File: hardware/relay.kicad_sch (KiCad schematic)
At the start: 0 parts

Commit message: Relay module completed
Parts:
- added D?: 1N4148, Diode_THT:D_DO-35_SOD27_P7.62mm_Horizontal, symbol Diode:1N4148
- added D?: LED_GREEN, symbol Device:LED
- added K?: G5LE-1, Relay_THT:Relay_SPDT_Omron-G5LE-1, symbol Relay:G5LE-1
- added Q?: BC847, Package_TO_SOT_SMD:SOT-23, symbol Transistor_BJT:BC847
- added R? (x2): 4K7, symbol Device:R_Small
- added R?: 47K, symbol Device:R_Small
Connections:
- new net: Q?.1 (B), R?.1, R?.2
- new net: D?.2 (A), K?.2, Q?.3 (C), R?.2
- new net: D?.2 (A), R?.1
- new net +12V: D?.1 (K), K?.5
- new net GND: D?.1 (K), Q?.2 (E), R?.2
- new net RELAY_CNT: R?.1
- new net RELAY_IN: K?.1
- new net RELAY_NC: K?.4
- new net RELAY_NO: K?.3

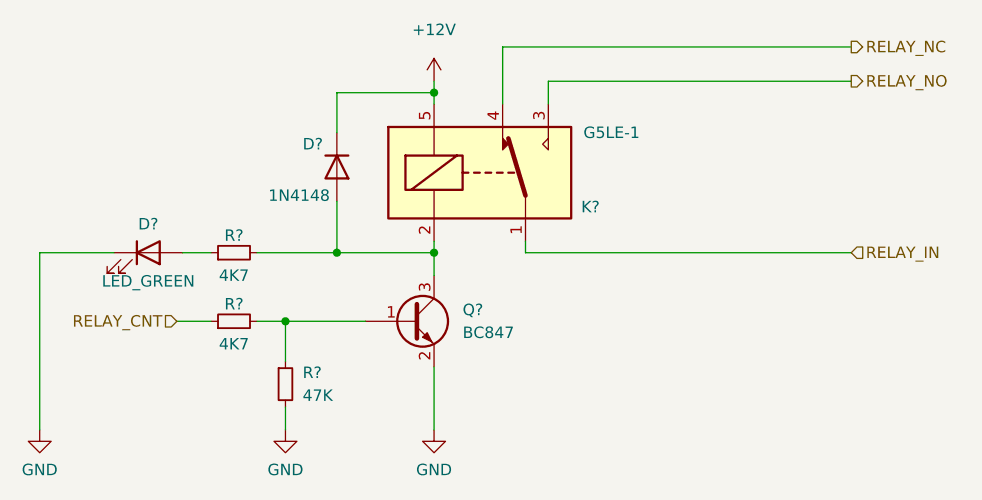
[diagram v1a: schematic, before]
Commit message: Display circuit added
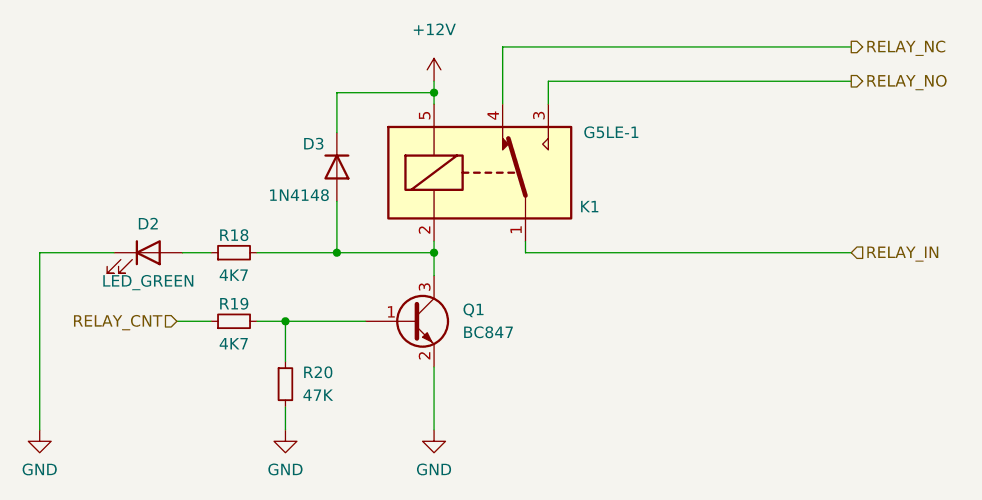
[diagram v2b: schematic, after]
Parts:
- gave numbers to parts that had none: 7
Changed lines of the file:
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@@
   (symbol (lib_id "power:GND") (at 109.22 107.95 0) (unit 1)
     (in_bom yes) (on_board yes) (fields_autoplaced)
-    (property "Reference" "#PWR?" (id 0) (at 109.22 114.3 0)
+    (property "Reference" "#PWR021" (id 0) (at 109.22 114.3 0)
       (effects (font (size 1.27 1.27)) hide)
     )
@@
   (symbol (lib_id "power:+12V") (at 153.035 69.215 0) (unit 1)
     (in_bom yes) (on_board yes) (fields_autoplaced)
-    (property "Reference" "#PWR?" (id 0) (at 153.035 73.025 0)
+    (property "Reference" "#PWR023" (id 0) (at 153.035 73.025 0)
       (effects (font (size 1.27 1.27)) hide)
     )
@@
   (symbol (lib_id "Device:R_Small") (at 130.81 95.885 90) (unit 1)
     (in_bom yes) (on_board yes)
-    (property "Reference" "R?" (id 0) (at 130.81 93.98 90))
+    (property "Reference" "R19" (id 0) (at 130.81 93.98 90))
     (property "Value" "4K7" (id 1) (at 130.81 98.425 90))
     (property "Footprint" "" (id 2) (at 130.81 95.885 0)
@@
   (symbol (lib_id "Relay:G5LE-1") (at 158.115 79.375 0) (unit 1)
     (in_bom yes) (on_board yes)
-    (property "Reference" "K?" (id 0) (at 171.45 83.185 0)
+    (property "Reference" "K1" (id 0) (at 171.45 83.185 0)
       (effects (font (size 1.27 1.27)) (justify right))
     )
@@
   (symbol (lib_id "Diode:1N4148") (at 142.24 78.74 270) (unit 1)
     (in_bom yes) (on_board yes)
-    (property "Reference" "D?" (id 0) (at 138.43 76.2 90)
+    (property "Reference" "D3" (id 0) (at 138.43 76.2 90)
       (effects (font (size 1.27 1.27)) (justify left))
     )
@@
   (symbol (lib_id "power:GND") (at 153.035 107.95 0) (unit 1)
     (in_bom yes) (on_board yes) (fields_autoplaced)
-    (property "Reference" "#PWR?" (id 0) (at 153.035 114.3 0)
+    (property "Reference" "#PWR024" (id 0) (at 153.035 114.3 0)
       (effects (font (size 1.27 1.27)) hide)
     )
@@
   (symbol (lib_id "Transistor_BJT:BC847") (at 150.495 95.885 0) (unit 1)
     (in_bom yes) (on_board yes) (fields_autoplaced)
-    (property "Reference" "Q?" (id 0) (at 156.21 94.6149 0)
+    (property "Reference" "Q1" (id 0) (at 156.21 94.6149 0)
       (effects (font (size 1.27 1.27)) (justify left))
     )
@@
   (symbol (lib_id "Device:LED") (at 121.285 88.265 0) (unit 1)
     (in_bom yes) (on_board yes)
-    (property "Reference" "D?" (id 0) (at 121.285 85.09 0))
+    (property "Reference" "D2" (id 0) (at 121.285 85.09 0))
     (property "Value" "LED_GREEN" (id 1) (at 121.285 91.44 0))
     (property "Footprint" "" (id 2) (at 121.285 88.265 0)
@@
   (symbol (lib_id "power:GND") (at 136.525 107.95 0) (unit 1)
     (in_bom yes) (on_board yes) (fields_autoplaced)
-    (property "Reference" "#PWR?" (id 0) (at 136.525 114.3 0)
+    (property "Reference" "#PWR022" (id 0) (at 136.525 114.3 0)
       (effects (font (size 1.27 1.27)) hide)
     )
@@
   (symbol (lib_id "Device:R_Small") (at 136.525 102.87 0) (unit 1)
     (in_bom yes) (on_board yes) (fields_autoplaced)
-    (property "Reference" "R?" (id 0) (at 138.43 101.5999 0)
+    (property "Reference" "R20" (id 0) (at 138.43 101.5999 0)
       (effects (font (size 1.27 1.27)) (justify left))
     )
@@
   (symbol (lib_id "Device:R_Small") (at 130.81 88.265 90) (unit 1)
     (in_bom yes) (on_board yes)
-    (property "Reference" "R?" (id 0) (at 130.81 86.36 90))
+    (property "Reference" "R18" (id 0) (at 130.81 86.36 90))
     (property "Value" "4K7" (id 1) (at 130.81 90.805 90))
     (property "Footprint" "" (id 2) (at 130.81 88.265 0)

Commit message: Schematics are completed
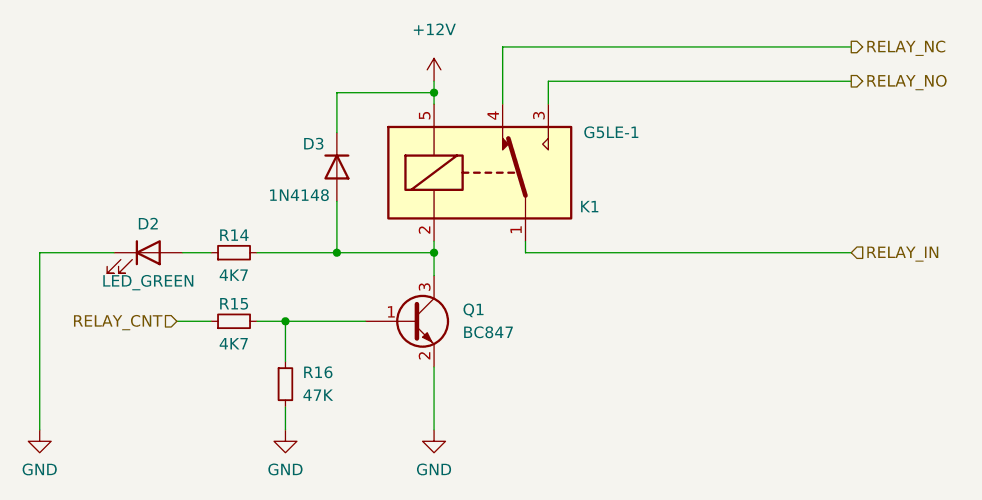
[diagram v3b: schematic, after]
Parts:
- D2: footprint (none) -> LED_SMD:LED_1206_3216Metric
- R14: renamed from R18; footprint (none) -> Resistor_SMD:R_0603_1608Metric
- R15: renamed from R19; footprint (none) -> Resistor_SMD:R_0603_1608Metric
- R16: renamed from R20; footprint (none) -> Resistor_SMD:R_0603_1608Metric
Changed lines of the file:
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@@
   (symbol (lib_id "power:GND") (at 109.22 107.95 0) (unit 1)
     (in_bom yes) (on_board yes) (fields_autoplaced)
-    (property "Reference" "#PWR021" (id 0) (at 109.22 114.3 0)
+    (property "Reference" "#PWR020" (id 0) (at 109.22 114.3 0)
       (effects (font (size 1.27 1.27)) hide)
     )
@@
   (symbol (lib_id "power:+12V") (at 153.035 69.215 0) (unit 1)
     (in_bom yes) (on_board yes) (fields_autoplaced)
-    (property "Reference" "#PWR023" (id 0) (at 153.035 73.025 0)
+    (property "Reference" "#PWR022" (id 0) (at 153.035 73.025 0)
       (effects (font (size 1.27 1.27)) hide)
     )
@@
   (symbol (lib_id "Device:R_Small") (at 130.81 95.885 90) (unit 1)
     (in_bom yes) (on_board yes)
-    (property "Reference" "R19" (id 0) (at 130.81 93.98 90))
+    (property "Reference" "R15" (id 0) (at 130.81 93.98 90))
     (property "Value" "4K7" (id 1) (at 130.81 98.425 90))
-    (property "Footprint" "" (id 2) (at 130.81 95.885 0)
+    (property "Footprint" "Resistor_SMD:R_0603_1608Metric" (id 2) (at 130.81 95.885 0)
       (effects (font (size 1.27 1.27)) hide)
     )
@@
   (symbol (lib_id "power:GND") (at 153.035 107.95 0) (unit 1)
     (in_bom yes) (on_board yes) (fields_autoplaced)
-    (property "Reference" "#PWR024" (id 0) (at 153.035 114.3 0)
+    (property "Reference" "#PWR023" (id 0) (at 153.035 114.3 0)
       (effects (font (size 1.27 1.27)) hide)
     )
@@
     (property "Reference" "D2" (id 0) (at 121.285 85.09 0))
     (property "Value" "LED_GREEN" (id 1) (at 121.285 91.44 0))
-    (property "Footprint" "" (id 2) (at 121.285 88.265 0)
+    (property "Footprint" "LED_SMD:LED_1206_3216Metric" (id 2) (at 121.285 88.265 0)
       (effects (font (size 1.27 1.27)) hide)
     )
@@
   (symbol (lib_id "power:GND") (at 136.525 107.95 0) (unit 1)
     (in_bom yes) (on_board yes) (fields_autoplaced)
-    (property "Reference" "#PWR022" (id 0) (at 136.525 114.3 0)
+    (property "Reference" "#PWR021" (id 0) (at 136.525 114.3 0)
       (effects (font (size 1.27 1.27)) hide)
     )
@@
   (symbol (lib_id "Device:R_Small") (at 136.525 102.87 0) (unit 1)
     (in_bom yes) (on_board yes) (fields_autoplaced)
-    (property "Reference" "R20" (id 0) (at 138.43 101.5999 0)
+    (property "Reference" "R16" (id 0) (at 138.43 101.5999 0)
       (effects (font (size 1.27 1.27)) (justify left))
     )
@@
       (effects (font (size 1.27 1.27)) (justify left))
     )
-    (property "Footprint" "" (id 2) (at 136.525 102.87 0)
+    (property "Footprint" "Resistor_SMD:R_0603_1608Metric" (id 2) (at 136.525 102.87 0)
       (effects (font (size 1.27 1.27)) hide)
     )
@@
   (symbol (lib_id "Device:R_Small") (at 130.81 88.265 90) (unit 1)
     (in_bom yes) (on_board yes)
-    (property "Reference" "R18" (id 0) (at 130.81 86.36 90))
+    (property "Reference" "R14" (id 0) (at 130.81 86.36 90))
     (property "Value" "4K7" (id 1) (at 130.81 90.805 90))
-    (property "Footprint" "" (id 2) (at 130.81 88.265 0)
+    (property "Footprint" "Resistor_SMD:R_0603_1608Metric" (id 2) (at 130.81 88.265 0)
       (effects (font (size 1.27 1.27)) hide)
     )
